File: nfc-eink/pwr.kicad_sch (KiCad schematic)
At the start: 19 parts, among them U2 TPS61023DRLR, U3 TPS22917DBVR, U4 TCM809SENB713

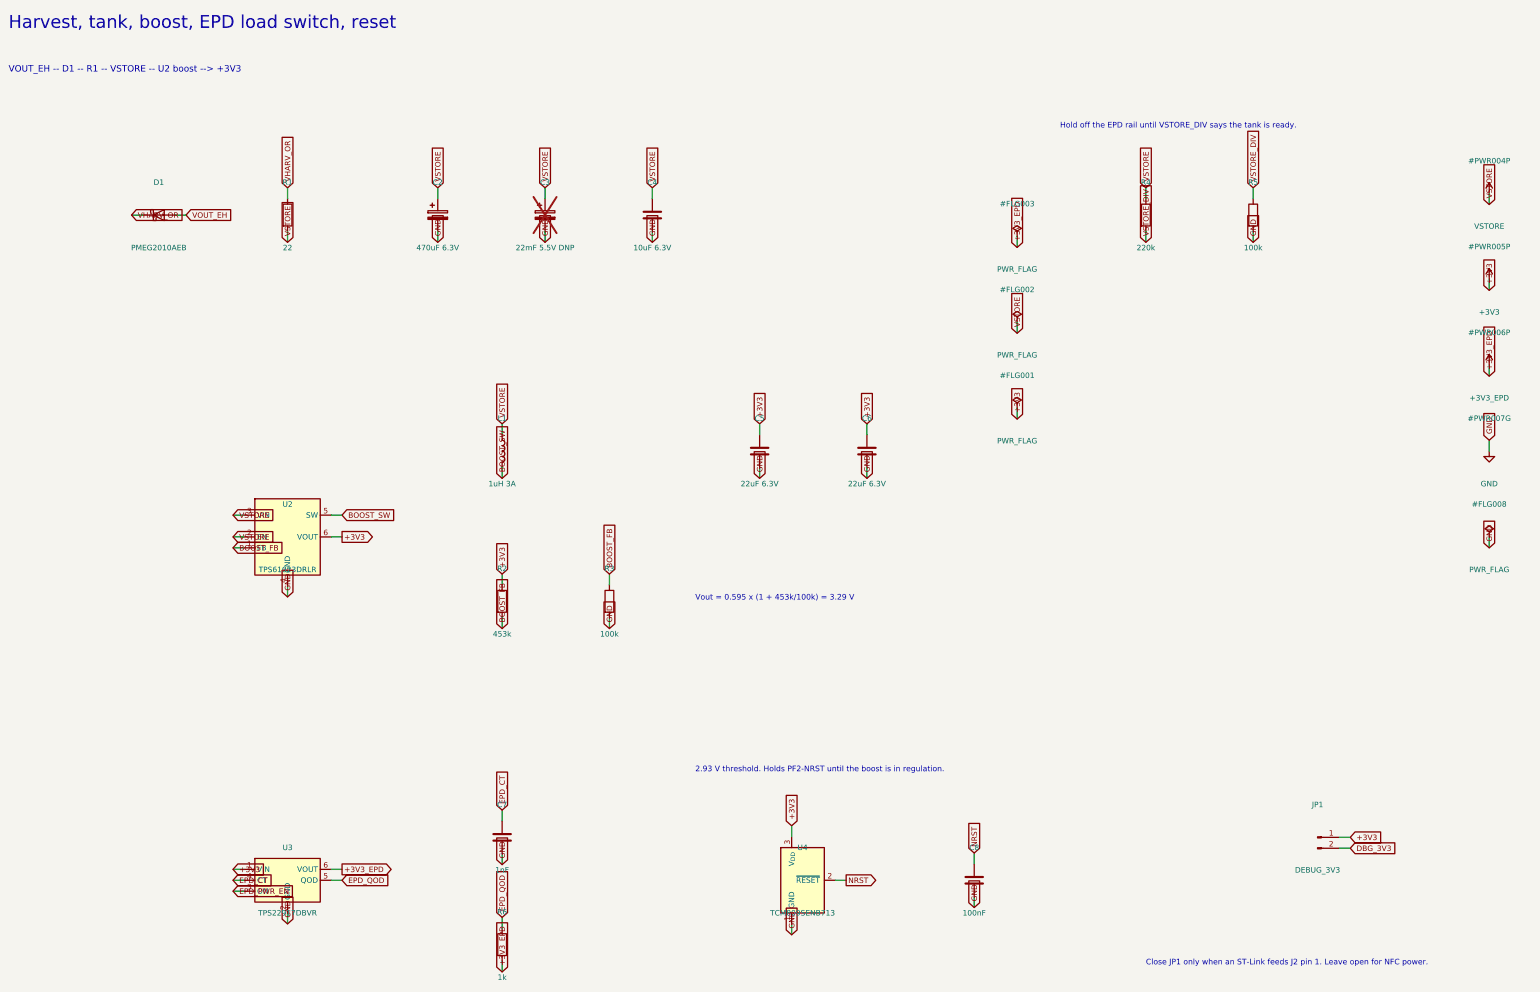
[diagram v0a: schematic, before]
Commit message: Fix first-article failures in the NFC e-ink design
The NTAG session masks were swapped, so pass-through never enabled
and the mailbox polled I2C_LOCKED. Hold EPD_PWR_EN and NRST at
reset, drop the push-pull reset cap, and use a low-profile tank so
a phone can sit on the coil.

Co-authored-by: Jason Hall <imjasonh@users.noreply.github.com>
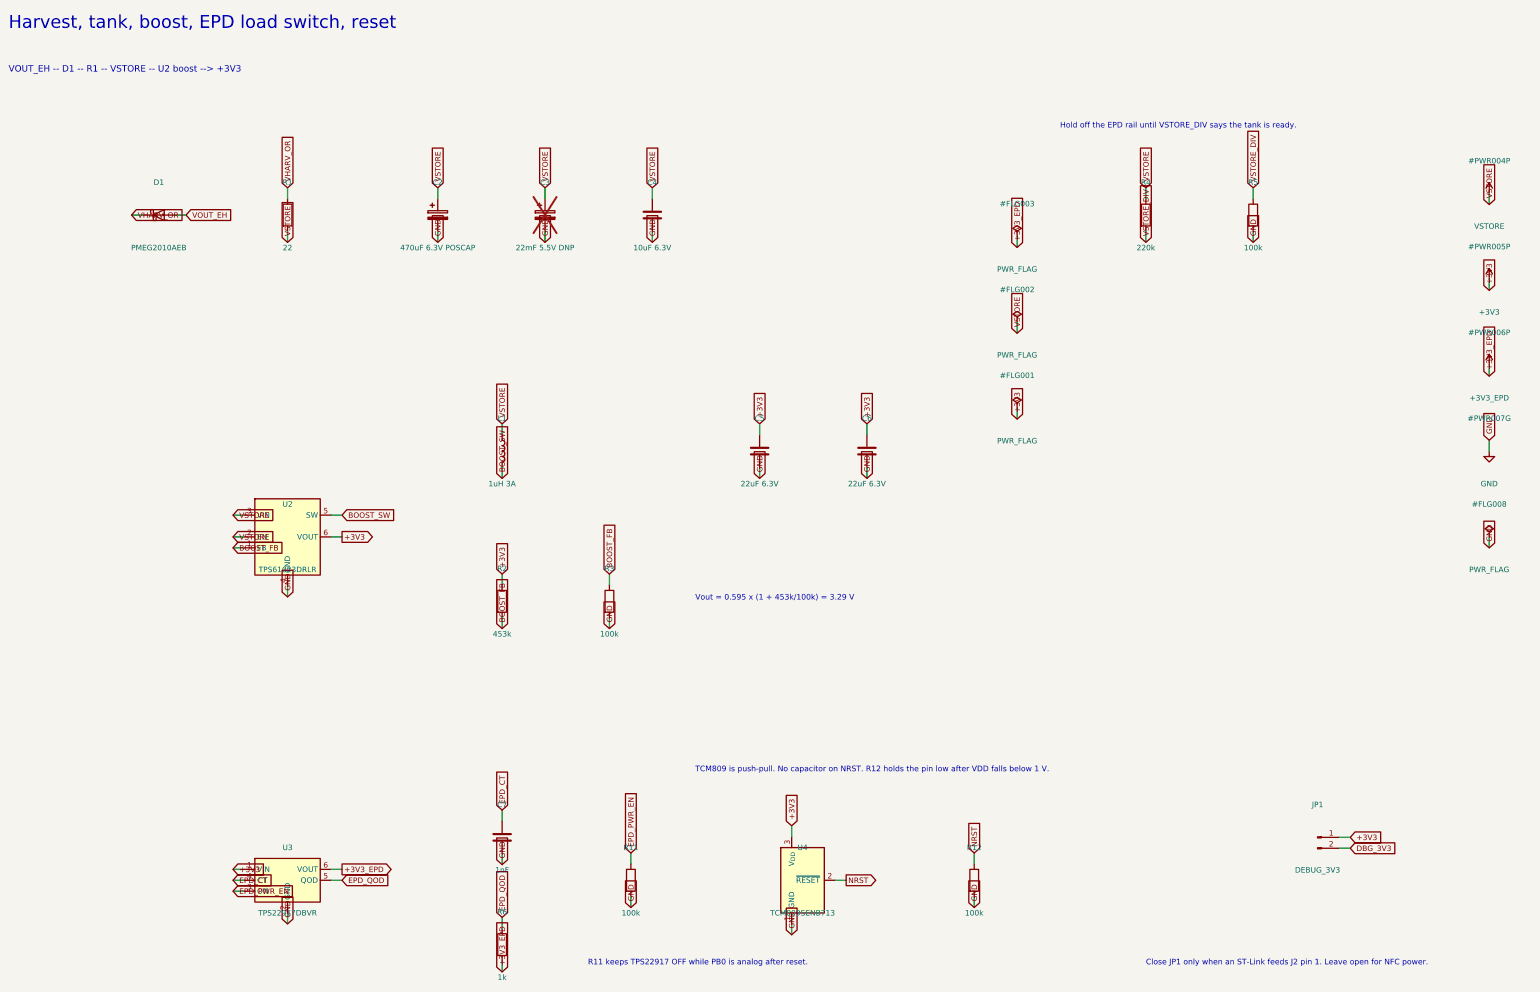
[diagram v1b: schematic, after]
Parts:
- removed C8: 100nF, Capacitor_SMD:C_0402_1005Metric, symbol Device:C
- added R11, R12: 100k, Resistor_SMD:R_0402_1005Metric, symbol Device:R
- C2: value 470uF 6.3V -> 470uF 6.3V POSCAP; footprint Capacitor_THT:CP_Radial_D8.0mm_P3.50mm -> Capacitor_Tantalum_SMD:CP_EIA-7343-20_Kemet-V; MPN 6SEPC470M -> 6TPE470MAZB
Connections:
- net EPD_PWR_EN: now also R11.1
- net GND: now also R11.2, R12.2
- net NRST: now also R12.1
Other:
- note added: "R11 keeps TPS22917 OFF while PB0 is analog after reset."
- note added: "TCM809 is push-pull. No capacitor on NRST. R12 holds the pin low after VDD falls below 1 V."
- note removed: "2.93 V threshold. Holds PF2-NRST until the boost is in regulation."
